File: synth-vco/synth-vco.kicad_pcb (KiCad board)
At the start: 4 copper layers, 146 parts, among them J1 Conn_Coaxial, J2 Screw_Terminal_01x02, J4 Conn_Coaxial, J6 Conn_02x09_Odd_Even, U1 ADF4158, U10 LT3045IMSE_TRPBF, U11 LT3045IMSE_TRPBF, U12 LT3045IMSE_TRPBF, U13 LT8570EMS8E_TRPBF, U14 LT3065EDDPBF, U15 LT3065EDDPBF, U16 BT09E, U3 ADP-2-10+, U4 DAT-15R5A-SP+, U5 OPA192IDGKT, U6 TPSM53602RDAR, U7 LT3045IMSE_TRPBF, U8 LT3045IMSE_TRPBF, U9 LT3045IMSE_TRPBF, Y1 FT3MN 26 MHz, Y3 CVCO55CW-0500-1000

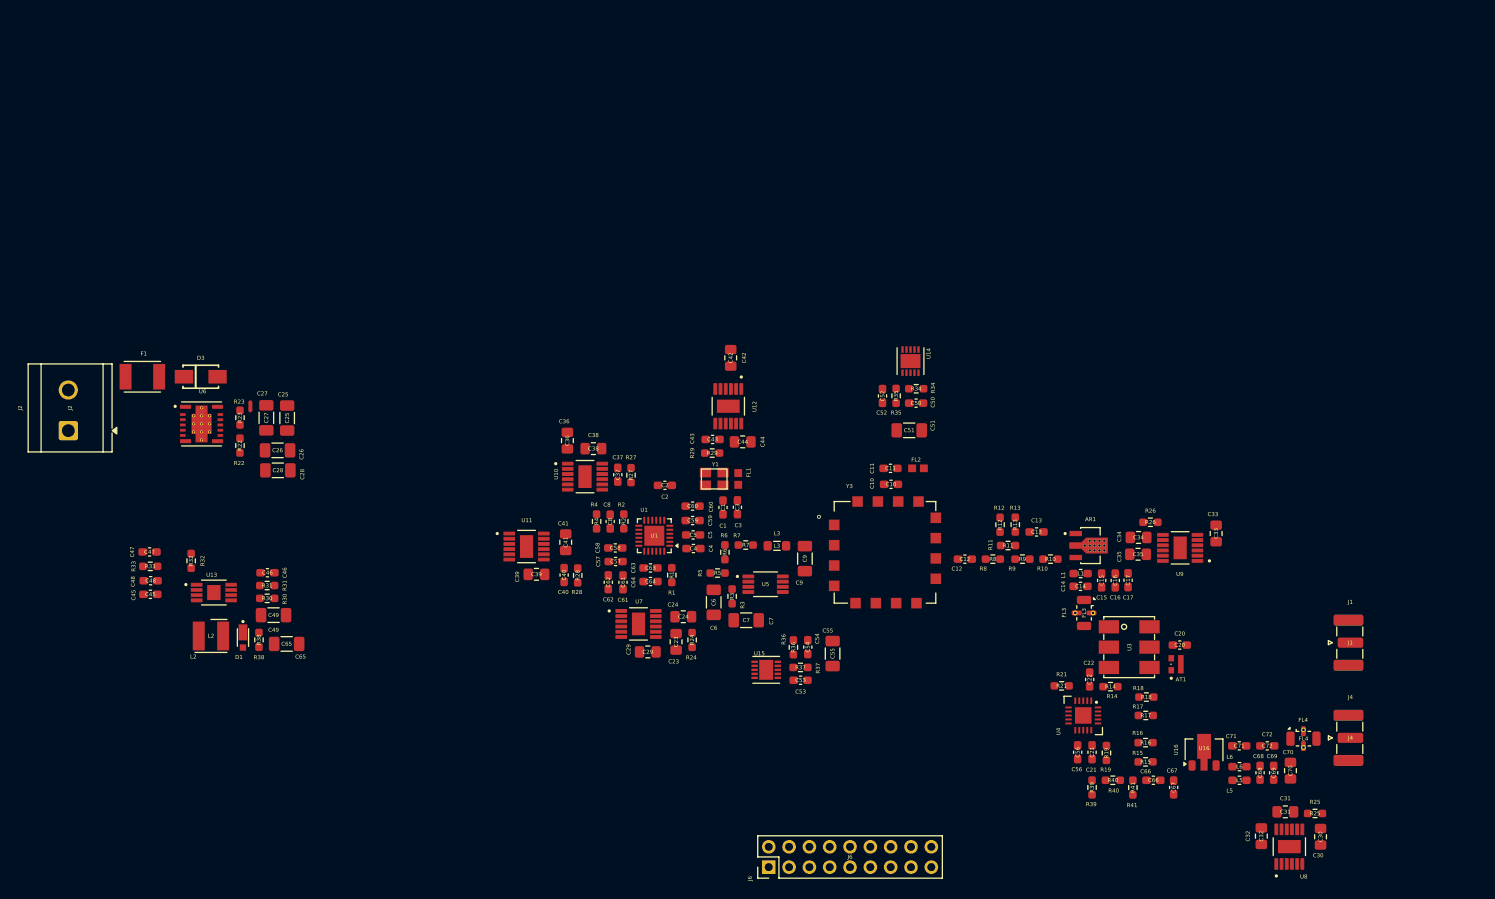
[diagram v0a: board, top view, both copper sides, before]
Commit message: feat(power blocks): pcb layout of power blocks
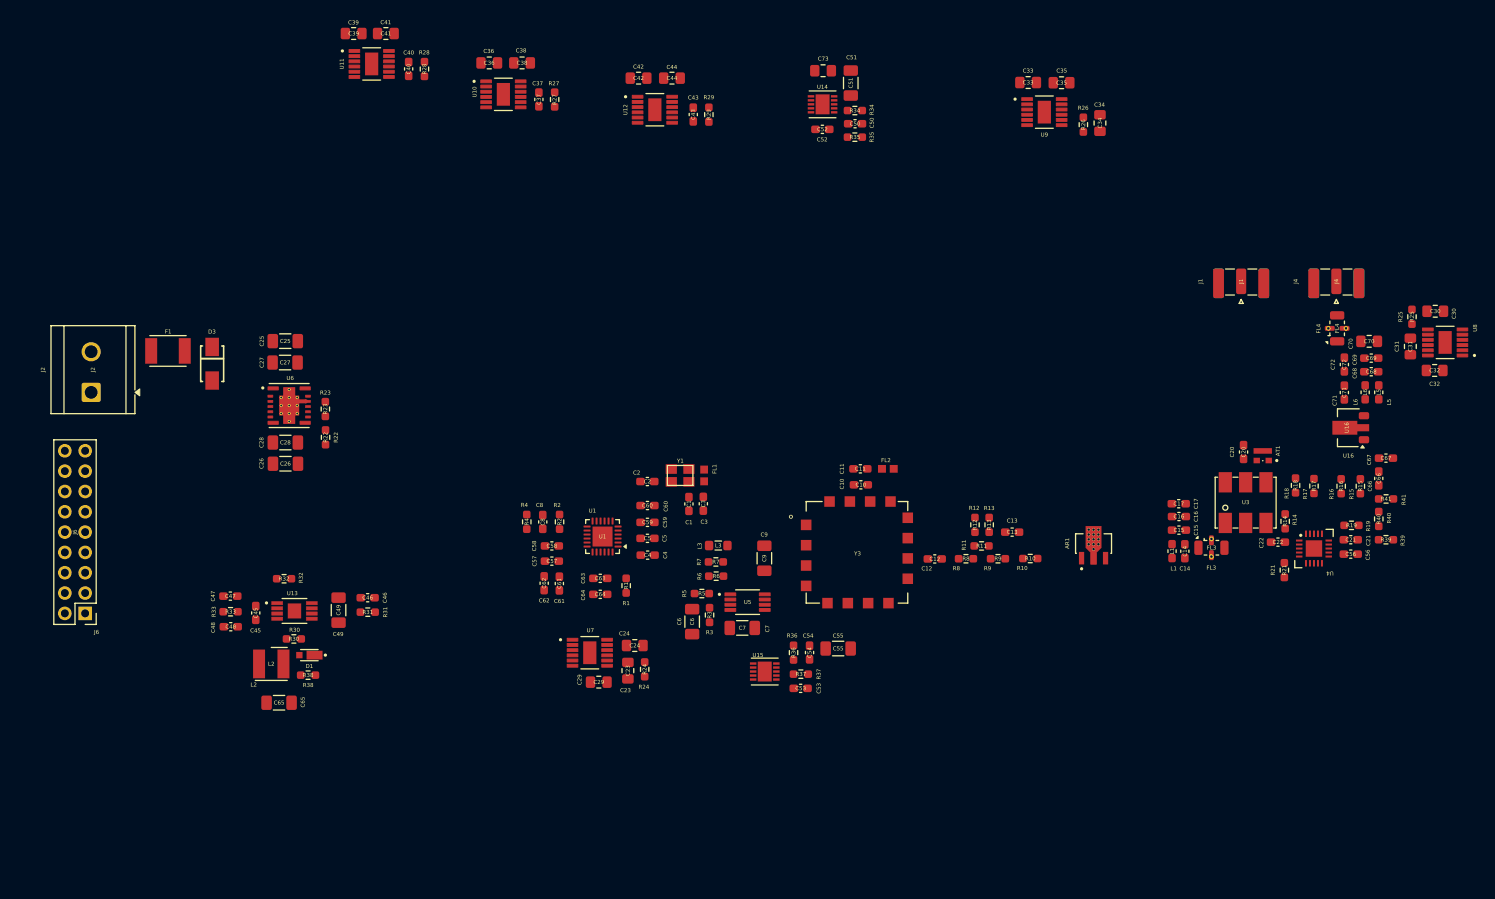
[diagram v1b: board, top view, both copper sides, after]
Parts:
- added C73: 2.2u, Capacitor_SMD:C_0805_2012Metric_Pad1.18x1.45mm_HandSolder, F.Cu at (135.3, 21.2)
- moved J6 91.1 mm to (43.0, 89.1), turned to 180 degrees
- moved C39 71.4 mm to (76.6, 16.6), turned to 180 degrees
- moved C41 67.4 mm to (80.6, 16.6), turned to 0 degrees
- moved C30 67.2 mm to (211.8, 51.3), turned to 180 degrees
- moved C40 66.2 mm to (83.5, 21.0), turned to -90 degrees
- moved R28 66.1 mm to (85.5, 21.0), turned to 90 degrees
- moved U8 66.0 mm to (213.1, 55.2), turned to 180 degrees
- moved U11 63.4 mm to (78.9, 20.4)
- moved R25 63.3 mm to (208.9, 52.0), turned to 90 degrees
- moved C32 62.1 mm to (211.7, 58.7), turned to 180 degrees
- moved C33 61.1 mm to (160.9, 22.7), turned to 180 degrees
- moved C31 60.2 mm to (208.7, 55.7), turned to 90 degrees
- moved C35 59.7 mm to (165.1, 22.8)
- moved J4 57.1 mm to (199.4, 47.6), turned to 90 degrees
- moved U9 57.0 mm to (162.9, 26.4), turned to 0 degrees
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
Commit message: feat(rf layout): rf track pcb layout kind of completed
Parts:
- removed C21: 100pF, Capacitor_SMD:C_0603_1608Metric_Pad1.08x0.95mm_HandSolder
- removed R39, R41: 100, Resistor_SMD:R_0603_1608Metric_Pad0.98x0.95mm_HandSolder
- removed R40: 68, Resistor_SMD:R_0603_1608Metric_Pad0.98x0.95mm_HandSolder
- added C18: 100nF, Capacitor_SMD:C_0603_1608Metric_Pad1.08x0.95mm_HandSolder, F.Cu at (76.1, 88.4)
- added C74: 2.2u, Capacitor_SMD:C_0805_2012Metric_Pad1.18x1.45mm_HandSolder, F.Cu at (135.4, 34.0)
- moved C23 118.4 mm to (202.8, 21.6), turned to -90 degrees
- moved C29 118.4 mm to (193.8, 16.9), turned to 180 degrees
- moved U7 115.7 mm to (195.6, 20.6)
- moved C24 115.0 mm to (197.8, 16.9), turned to 0 degrees
- moved R24 114.8 mm to (200.7, 21.9), turned to 90 degrees
- moved C70 101.3 mm to (109.2, 92.0), turned to 180 degrees
- moved C69 100.4 mm to (109.0, 90.0), turned to 180 degrees
- moved C68 99.3 mm to (108.9, 88.2), turned to 180 degrees
- moved L5 99.0 mm to (108.9, 86.5), turned to 180 degrees
- moved C67 94.5 mm to (111.6, 78.9), turned to 0 degrees
- moved L6 94.2 mm to (112.5, 87.3), turned to -90 degrees
- moved C71 92.7 mm to (112.5, 90.8)
- moved C66 92.3 mm to (112.5, 76.2), turned to -90 degrees
- moved C56 91.6 mm to (109.8, 75.5), turned to 180 degrees
- moved C72 91.2 mm to (115.0, 90.0), turned to 0 degrees
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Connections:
- C66 pad 1: Net-(C66-Pad1) -> Net-(U4-RFout)
- L3 pad 1: Net-(L3-Pad1) -> Net-(Y3-VT)
- L3 pad 2: Net-(Y3-VT) -> Net-(L3-Pad2)
- R7 pad 2: Net-(L3-Pad1) -> Net-(L3-Pad2)

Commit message: feat: positioned power blocks
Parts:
- moved C24 124.0 mm to (112.6, 107.0)
- moved U7 124.0 mm to (110.3, 110.6)
- moved C29 124.0 mm to (108.5, 107.0)
- moved R24 123.7 mm to (115.1, 111.3)
- moved C23 123.7 mm to (117.3, 111.1)
- moved C30 91.4 mm to (158.4, 106.4)
- moved C32 91.4 mm to (162.3, 106.4)
- moved U8 91.4 mm to (160.3, 110.0)
- moved C31 90.8 mm to (166.9, 110.4)
- moved R25 90.8 mm to (164.8, 110.6)
- moved C41 84.3 mm to (112.5, 94.6), turned to -90 degrees
- moved C39 82.3 mm to (112.5, 90.6), turned to 90 degrees
- moved R28 81.6 mm to (108.1, 99.5), turned to 0 degrees
- moved C40 80.3 mm to (108.1, 97.5), turned to 180 degrees
- moved C38 78.9 mm to (128.4, 89.3), turned to -90 degrees
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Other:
- board outline added: 91.8 x 61.8 mm

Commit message: refactor: switched to wurth box header
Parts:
- removed J6: Conn_02x09_Odd_Even, Connector_PinHeader_2.54mm:PinHeader_2x09_P2.54mm_Vertical
- added J3: 61202021621, GPR_Radar_Footprints:J_Wurth_WR-BHD_61202021621, F.Cu at (96.4, 85.4)

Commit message: feat: routing and polygons
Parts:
- added R45: 500K, Resistor_SMD:R_0603_1608Metric_Pad0.98x0.95mm_HandSolder, F.Cu at (138.8, 73.6)
- added R46: 500K, Resistor_SMD:R_0603_1608Metric_Pad0.98x0.95mm_HandSolder, F.Cu at (145.4, 112.1)
- moved C18 4.98 mm to (130.2, 102.9), turned to 180 degrees
- moved R7 4.94 mm to (133.9, 102.9), turned to 0 degrees
- moved C63 4.71 mm to (120.7, 107.1)
- moved U12 4.49 mm to (109.3, 84.3)
- moved C42 4.41 mm to (107.3, 80.4)
- moved C44 4.29 mm to (111.6, 80.4)
- moved R29 4.29 mm to (116.2, 84.9)
- moved C43 4.29 mm to (114.3, 84.9)
- moved C64 4.14 mm to (120.7, 105.3)
- moved R6 3.93 mm to (136.8, 106.8)
- moved R1 3.90 mm to (124.3, 106.3)
- moved R5 3.88 mm to (135.2, 106.8)
- moved U5 3.88 mm to (132.1, 107.1)
- moved R3 3.14 mm to (132.6, 112.2)
- moved C36 2.53 mm to (128.4, 82.6)
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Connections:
- J3 pad 1: /SPI_CLK -> /PLL_TXDATA
- J3 pad 13: /ATT_CLK -> /ATT_LE
- J3 pad 15: /ATT_DATA -> /ATT_CLK
- J3 pad 17: /ATT_LE -> /ATT_DATA
- J3 pad 3: /SPI_DATA -> /PLL_CE
- J3 pad 5: /PLL_LE -> /SPI_CLK
- J3 pad 7: /PLL_CE -> /SPI_DATA
- J3 pad 9: /PLL_TXDATA -> /PLL_LE
- U14 pad 4: unconnected-(U14-PWRGD-Pad4) -> Net-(U14-PWRGD)
- U15 pad 4: unconnected-(U15-PWRGD-Pad4) -> Net-(U15-PWRGD)
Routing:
- net +6V_PRE: track 0.00 -> 215.1 mm, vias 0 -> 34
- net +20V_PRE: track 0.00 -> 133.7 mm, vias 0 -> 8
- net +3V3_PLL_D: track 0.00 -> 108.5 mm, vias 0 -> 14
- net /ATT_DATA: track 0.00 -> 85.2 mm, vias 0 -> 1
- net /ATT_LE: track 0.00 -> 84.4 mm, vias 0 -> 1
- net /ATT_CLK: track 0.00 -> 83.7 mm, vias 0 -> 1
- net +12V_IN: track 0.00 -> 54.0 mm, vias 0 -> 8
- net /PLL_TXDATA: track 0.00 -> 30.3 mm, vias 0 -> 1
- net /PLL_CE: track 0.00 -> 28.6 mm, vias 0 -> 1
- net Net-(C5-Pad2): track 0.00 -> 28.6 mm
- net /SPI_CLK: track 0.00 -> 28.1 mm, vias 0 -> 1
- net /SPI_DATA: track 0.00 -> 26.9 mm, vias 0 -> 1
- net +3V3_TCXO: track 0.00 -> 26.9 mm
- net /PLL_LE: track 0.00 -> 26.4 mm, vias 0 -> 1
- net +18V_OPA: track 0.00 -> 22.3 mm, vias 0 -> 3
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- added copper zone on B.Cu, net (none)
- added copper zone on F.Cu, net GND
- added copper zone on In1.Cu, net GND
- added copper zone on In2.Cu, net GND

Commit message: feat: fixed all of the drc errors and warnings
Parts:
- moved NT1 1.51 mm to (124.2, 59.3)
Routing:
- net +6V_PRE: track 215.1 -> 219.1 mm, vias 34 -> 36
- net +20V_PRE: track 133.7 -> 135.6 mm
- net Net-(U6-AGND): track 2.50 -> 1.97 mm
- added copper zone on B.Cu, net GND
- removed copper zone on B.Cu, net (none)

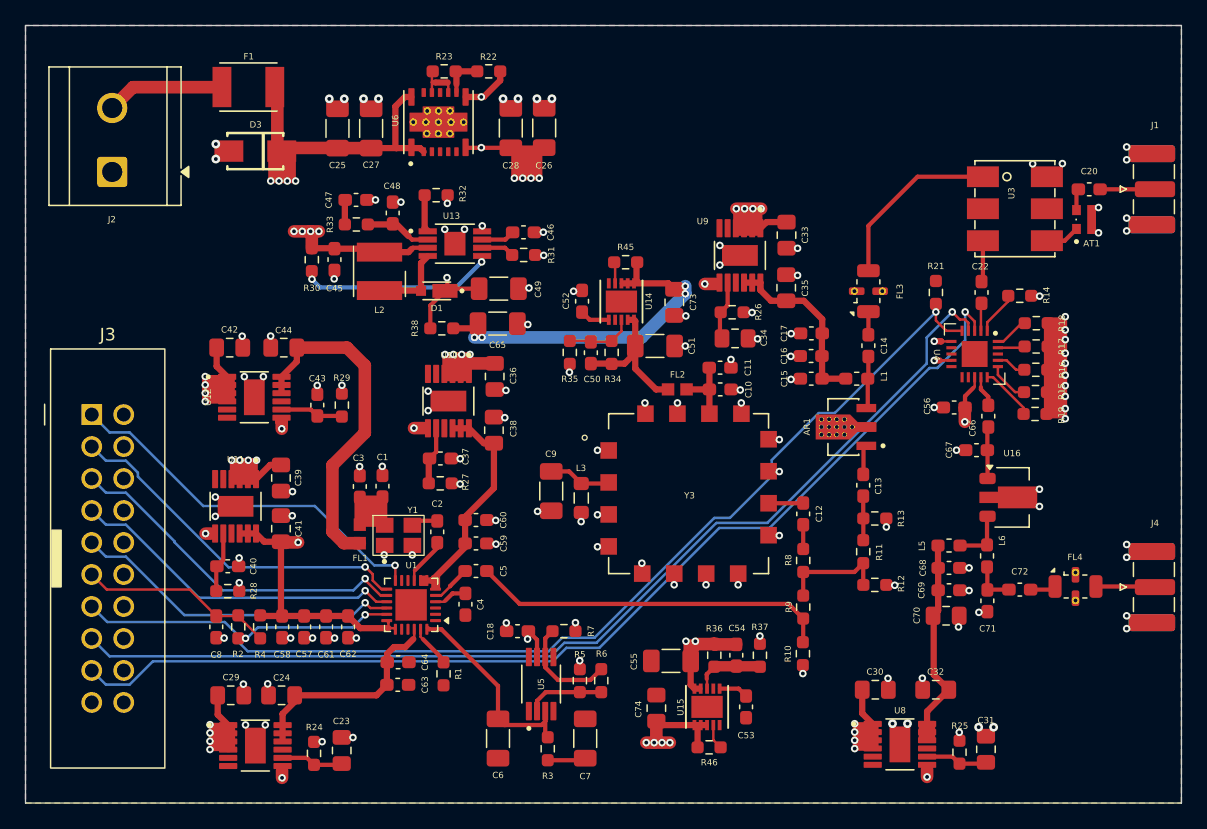
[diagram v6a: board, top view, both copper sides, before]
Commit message: feat: via stitching
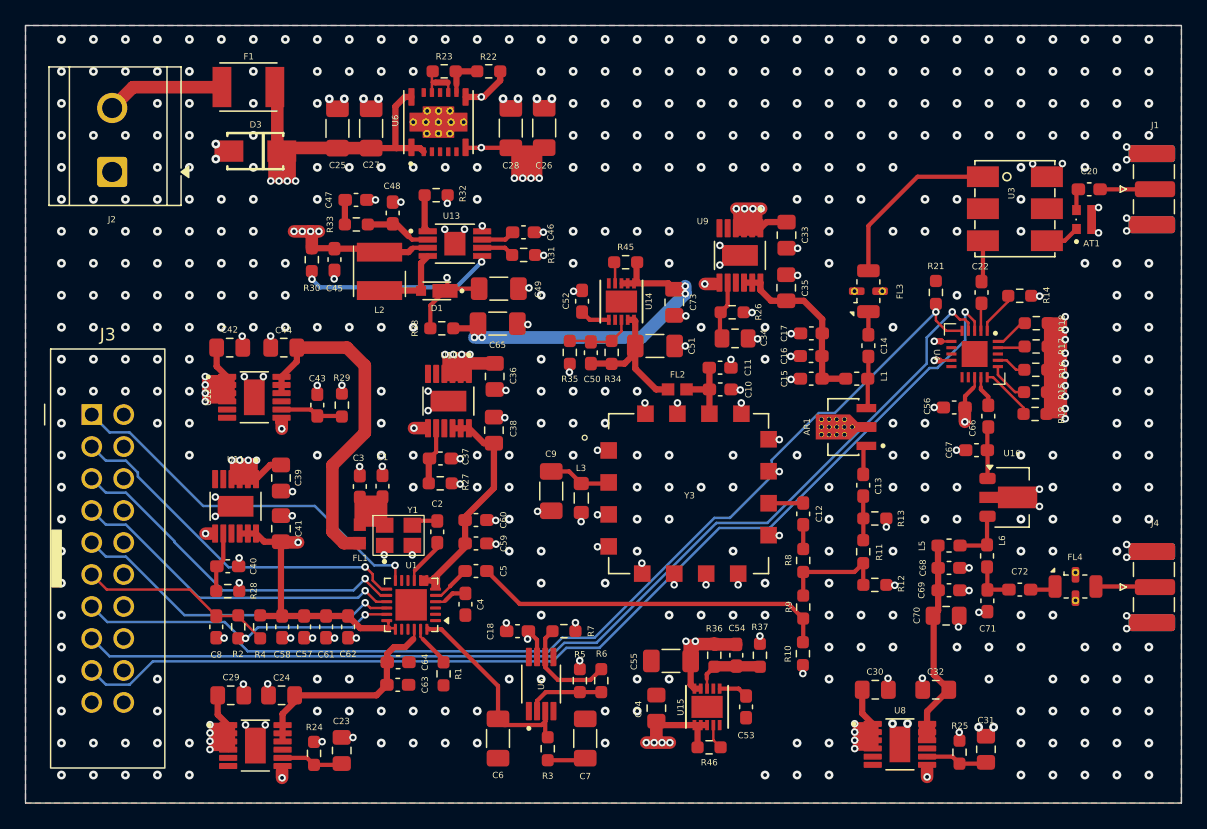
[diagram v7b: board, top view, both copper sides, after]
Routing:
- net GND: vias 118 -> 501
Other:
- board text added: "{ "ViaStitcher": "0.3.1", "GND_1": { "HSpacing": "2.54", "VSpacing": "2.54", "HOffset": "0", "VOffset": "0", "Clearance": "0", "Randomize": false, "Stagger": false, "OnlyFilledCopper": true } }"

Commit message: fix: added 10K resistor at DATA line for DAT-15R5A-SP+ in accordance with the datasheet
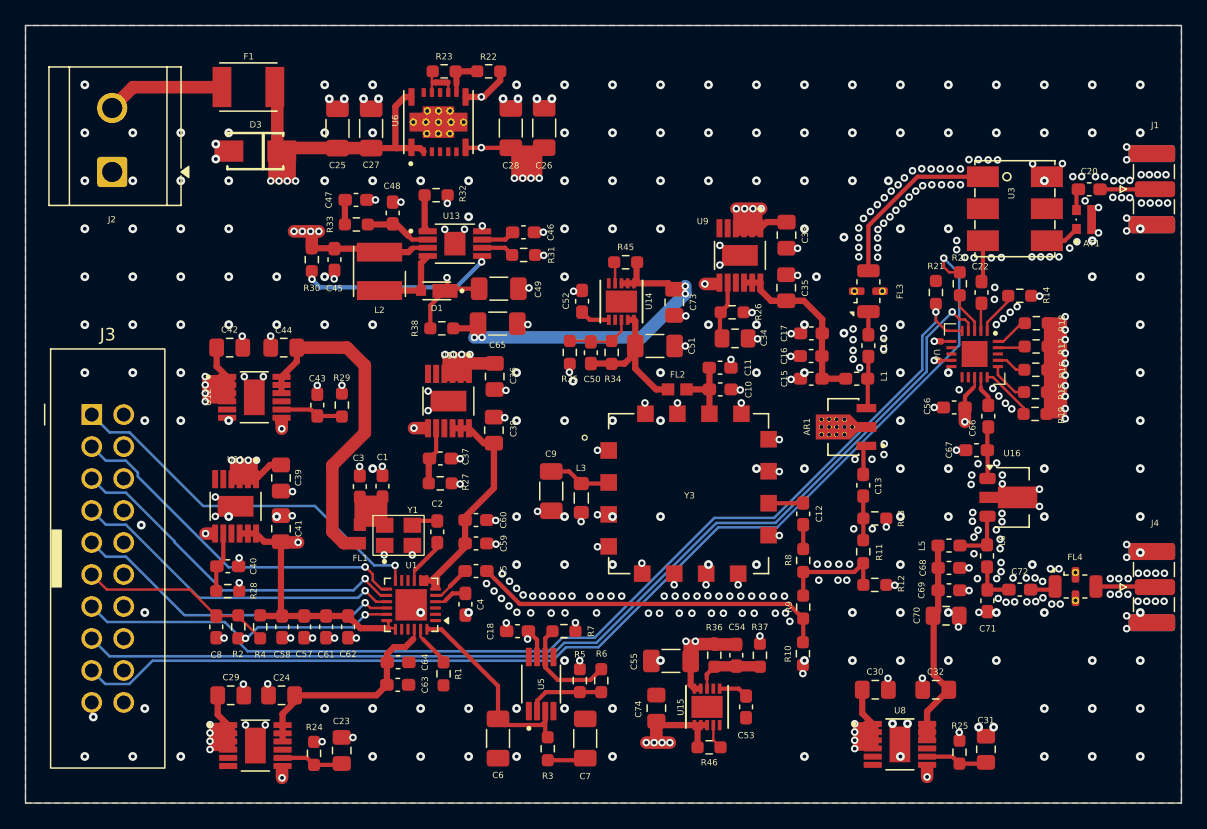
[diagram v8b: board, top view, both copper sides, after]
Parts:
- added R20: 10K, Resistor_SMD:R_0603_1608Metric_Pad0.98x0.95mm_HandSolder, F.Cu at (165.3, 75.3)
- F1: value MF-MSMF200 -> MF-MSMF200/16X
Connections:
- U4 pad 3: /ATT_DATA -> Net-(U4-DATA)
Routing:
- net /ATT_DATA: track 85.2 -> 90.1 mm
- net Net-(U4-DATA): track 0.00 -> 3.31 mm
- net /ATT_LE: track 84.4 -> 85.7 mm
- net GND: vias 501 -> 489
